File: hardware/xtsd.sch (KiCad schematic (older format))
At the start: 28 parts, among them J1 Bus_ISA_8bit_AB_Rev0, J2 SD_Card, J3 Micro_SD_Card, J4 Conn_01x02_Male, SW1 SW_DIP_x08, U1 74LS688, U2 74LS688, U3 SST39SF010, U4 74LS595, U5 74LS165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

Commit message: As ordered
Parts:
- J4: footprint Connector_PinHeader_2.54mm:PinHeader_1x02_P2.54mm_Horizontal -> Connector_PinHeader_2.54mm:PinHeader_1x02_P2.54mm_Vertical
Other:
- note added: "28C256"
- note added: "PIN 29 = PIN 27 /WE for 28C256\nPIN 3 = PIN 1 = A14 for 28C256"
- note removed: "28C64"
- note removed: "Check:\n-unused 4050 gates\n-shield pins SD card"
- note removed: "PIN 29 = PIN 27 /WE for 28C64 / 28C256\nPIN 3 = PIN 1 = A14 for 28C256"
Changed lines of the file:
@@
 encoding utf-8
 Sheet 1 1
-Title ""
+Title "XTSD XT ISA SD card interface"
 Date ""
 Rev ""
@@
 P 10300 3500
 F 0 "#PWR0103" H 10300 3250 50  0001 C CNN
-F 1 "GND" H 10305 3327 50  0000 C CNN
+F 1 "GND" H 10250 3350 50  0000 C CNN
 F 2 "" H 10300 3500 50  0001 C CNN
 F 3 "" H 10300 3500 50  0001 C CNN
@@
 	7600 2900 7600 3100
 Connection ~ 6500 2900
-Text Notes 2850 5900 0    50   ~ 0
-Check:\n-unused 4050 gates\n-shield pins SD card
 Wire Wire Line
 	3200 2100 3650 2100
@@
 F 0 "J4" H 6108 7081 50  0000 C CNN
 F 1 "Conn_01x02_Male" H 6108 6990 50  0000 C CNN
-F 2 "Connector_PinHeader_2.54mm:PinHeader_1x02_P2.54mm_Horizontal" H 6000 6900 50  0001 C CNN
+F 2 "Connector_PinHeader_2.54mm:PinHeader_1x02_P2.54mm_Vertical" H 6000 6900 50  0001 C CNN
 F 3 "~" H 6000 6900 50  0001 C CNN
 	1    6000 6900
@@
 U 1 1 6279998C
 P 10300 2300
-F 0 "U3" H 10300 3781 50  0000 C CNN
-F 1 "SST39SF010" H 10300 3690 50  0000 C CNN
+F 0 "U3" H 10500 1100 50  0000 C CNN
+F 1 "SST39SF010" H 10700 1000 50  0000 C CNN
 F 2 "Package_DIP:DIP-32_W15.24mm_Socket_LongPads" H 10300 2600 50  0001 C CNN
 F 3 "http://ww1.microchip.com/downloads/en/DeviceDoc/25022B.pdf" H 10300 2600 50  0001 C CNN
@@
 $EndComp
 Text Notes 8800 3600 0    50   ~ 0
-PIN 29 = PIN 27 /WE for 28C64 / 28C256\nPIN 3 = PIN 1 = A14 for 28C256
+PIN 29 = PIN 27 /WE for 28C256\nPIN 3 = PIN 1 = A14 for 28C256
 Wire Wire Line
 	5450 2700 5300 2700
@@
 	7700 2000 7200 2000
 Wire Bus Line
-	2950 800  7250 800
+	2950 750  7250 750
 $Comp
 L Jumper:SolderJumper_3_Open JP1
@@
 	0    -1   -1   0
 $EndComp
-Connection ~ 7250 800
+Connection ~ 7250 750
 Text Notes 9200 2850 2    50   ~ 0
-28C64
+28C256
 Text Notes 9250 1950 2    50   ~ 0
 39F010
@@
 FL_A15
 Wire Bus Line
-	7250 800  9400 800
+	7250 750  9400 750
 Wire Wire Line
 	9450 2800 9700 2800
@@
 Wire Wire Line
 	2750 7250 3150 7250
+Connection ~ 3950 7250
+Connection ~ 3150 7250
+Wire Wire Line
+	3150 7250 3350 7250
+Connection ~ 3350 7250
+Wire Wire Line
+	3350 7250 3550 7250
+Connection ~ 3550 7250
+Wire Wire Line
+	3550 7250 3950 7250
 Wire Bus Line
-	7250 800  7250 1800
+	7250 750  7250 1800
 Wire Bus Line
 	4800 3700 4800 5050
@@
 	2700 650  2700 2000
 Wire Bus Line
-	9400 800  9400 2400
+	9400 750  9400 2300
 Wire Bus Line
 	11100 650  11100 3700
 Wire Bus Line
-	2950 800  2950 4650
-Connection ~ 3950 7250
-Connection ~ 3150 7250
-Wire Wire Line
-	3150 7250 3350 7250
-Connection ~ 3350 7250
-Wire Wire Line
-	3350 7250 3550 7250
-Connection ~ 3550 7250
-Wire Wire Line
-	3550 7250 3950 7250
+	2950 750  2950 4650
 $EndSCHEMATC

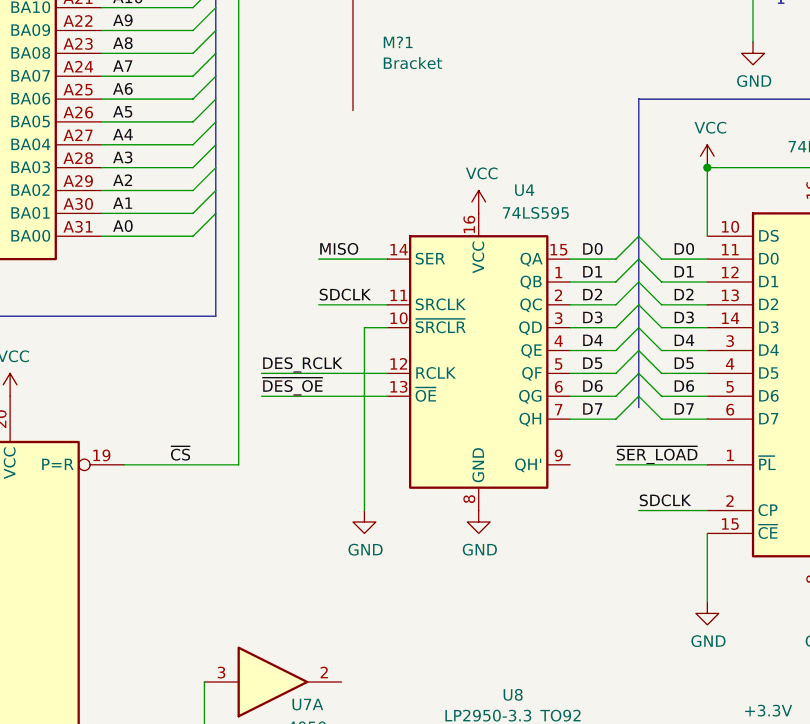
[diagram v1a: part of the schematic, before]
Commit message: fix: U4 /SRCLR should be connected to VCC instead of GND
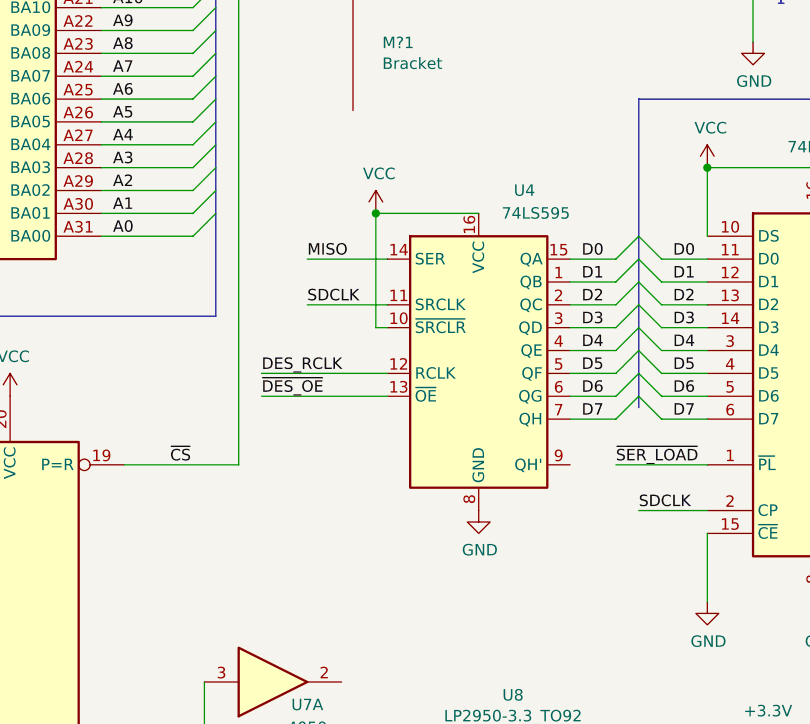
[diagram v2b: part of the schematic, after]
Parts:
- J4: footprint Connector_PinHeader_2.54mm:PinHeader_1x02_P2.54mm_Vertical -> Connector_PinHeader_2.54mm:PinHeader_1x02_P2.54mm_Horizontal
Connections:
- wire segments 316 -> 317
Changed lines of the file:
@@
 Text Label 4800 5500 0    50   ~ 0
 SDCLK
-Text Label 3400 4600 0    50   ~ 0
+Text Label 3350 4600 0    50   ~ 0
 SDCLK
 $Comp
@@
 	1    0    0    -1
 $EndComp
-$Comp
-L power:GND #PWR0112
-U 1 1 6270EEF5
-P 3600 5500
-F 0 "#PWR0112" H 3600 5250 50  0001 C CNN
-F 1 "GND" H 3605 5327 50  0000 C CNN
-F 2 "" H 3600 5500 50  0001 C CNN
-F 3 "" H 3600 5500 50  0001 C CNN
-	1    3600 5500
-	1    0    0    -1
-$EndComp
-Wire Wire Line
-	3600 5500 3600 4700
-Wire Wire Line
-	3600 4700 3700 4700
 Text Label 4950 4400 0    50   ~ 0
 D0
@@
 L power:VCC #PWR0118
 U 1 1 62BCA5EB
-P 4100 4200
-F 0 "#PWR0118" H 4100 4050 50  0001 C CNN
-F 1 "VCC" H 4115 4373 50  0000 C CNN
-F 2 "" H 4100 4200 50  0001 C CNN
-F 3 "" H 4100 4200 50  0001 C CNN
-	1    4100 4200
+P 3650 4200
+F 0 "#PWR0118" H 3650 4050 50  0001 C CNN
+F 1 "VCC" H 3665 4373 50  0000 C CNN
+F 2 "" H 3650 4200 50  0001 C CNN
+F 3 "" H 3650 4200 50  0001 C CNN
+	1    3650 4200
 	1    0    0    -1
 $EndComp
@@
 	8350 4650 8250 4650
 Connection ~ 8250 4650
-Wire Wire Line
-	3700 4400 3400 4400
-Text Label 3400 4400 0    50   ~ 0
+Text Label 3350 4400 0    50   ~ 0
 MISO
-Wire Wire Line
-	3400 4600 3700 4600
 Wire Wire Line
 	8350 4750 7850 4750
@@
 	1    0    0    -1
 $EndComp
-$Comp
-L Connector:Conn_01x02_Male J4
-U 1 1 62FB6638
-P 6000 6900
-F 0 "J4" H 6108 7081 50  0000 C CNN
-F 1 "Conn_01x02_Male" H 6108 6990 50  0000 C CNN
-F 2 "Connector_PinHeader_2.54mm:PinHeader_1x02_P2.54mm_Vertical" H 6000 6900 50  0001 C CNN
-F 3 "~" H 6000 6900 50  0001 C CNN
-	1    6000 6900
-	1    0    0    -1
-$EndComp
 Wire Wire Line
 	6200 6250 6200 6350
@@
 Wire Wire Line
 	3550 7250 3950 7250
+$Comp
+L Connector:Conn_01x02_Male J4
+U 1 1 62FB6638
+P 6000 6900
+F 0 "J4" H 6108 7081 50  0000 C CNN
+F 1 "Conn_01x02_Male" H 6108 6990 50  0000 C CNN
+F 2 "Connector_PinHeader_2.54mm:PinHeader_1x02_P2.54mm_Horizontal" H 6000 6900 50  0001 C CNN
+F 3 "~" H 6000 6900 50  0001 C CNN
+	1    6000 6900
+	1    0    0    -1
+$EndComp
+Wire Wire Line
+	3700 4700 3650 4700
+Wire Wire Line
+	3650 4700 3650 4200
+Wire Wire Line
+	4100 4200 3650 4200
+Connection ~ 3650 4200
+Wire Wire Line
+	3350 4600 3700 4600
+Wire Wire Line
+	3350 4400 3700 4400
 Wire Bus Line
 	7250 750  7250 1800
